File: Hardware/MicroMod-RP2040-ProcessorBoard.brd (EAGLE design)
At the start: 22 x 22 mm, 47 parts, among them J1 MICROMOD-2222, U1 W25QXX128MBIT, U2 FSUSB30MUX_MSOP10, U3 RP2040, Y1 12MHz

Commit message: Rename nets to match MicroMod nomenclature
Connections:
- net ADC0 renamed A0
- net ADC1 renamed A1
- net GPIO0 renamed G0
- net GPIO1 renamed G1
- net GPIO2 renamed G2
- net GPIO3 renamed G3
- net GPIO9 renamed G9
- net SPI_!CS!/GPIO5 renamed SPI_!CS!/G5
- net SPI_CIPO/GPIO4 renamed SPI_CIPO/G4
- net SPI_COPI/GPIO7 renamed SPI_COPI/G7
- net SPI_SCK/GPIO6 renamed SPI_SCK/G6
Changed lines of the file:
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@@
 <layers>
 <layer number="1" name="Top" color="4" fill="1" visible="yes" active="yes"/>
-<layer number="2" name="Horz" color="1" fill="3" visible="yes" active="yes"/>
-<layer number="15" name="Vert" color="4" fill="6" visible="yes" active="yes"/>
+<layer number="2" name="Horz" color="1" fill="3" visible="no" active="yes"/>
+<layer number="15" name="Vert" color="4" fill="6" visible="no" active="yes"/>
 <layer number="16" name="Bottom" color="1" fill="1" visible="yes" active="yes"/>
 <layer number="17" name="Pads" color="2" fill="1" visible="yes" active="yes"/>
@@
 <layer number="23" name="tOrigins" color="15" fill="1" visible="yes" active="yes"/>
 <layer number="24" name="bOrigins" color="15" fill="1" visible="yes" active="yes"/>
-<layer number="25" name="tNames" color="7" fill="1" visible="yes" active="yes"/>
-<layer number="26" name="bNames" color="7" fill="1" visible="yes" active="yes"/>
-<layer number="27" name="tValues" color="7" fill="1" visible="yes" active="yes"/>
-<layer number="28" name="bValues" color="7" fill="1" visible="yes" active="yes"/>
-<layer number="29" name="tStop" color="7" fill="3" visible="yes" active="yes"/>
-<layer number="30" name="bStop" color="7" fill="6" visible="yes" active="yes"/>
-<layer number="31" name="tCream" color="7" fill="4" visible="yes" active="yes"/>
-<layer number="32" name="bCream" color="7" fill="5" visible="yes" active="yes"/>
-<layer number="33" name="tFinish" color="6" fill="3" visible="yes" active="yes"/>
-<layer number="34" name="bFinish" color="6" fill="6" visible="yes" active="yes"/>
-<layer number="35" name="tGlue" color="7" fill="4" visible="yes" active="yes"/>
-<layer number="36" name="bGlue" color="7" fill="5" visible="yes" active="yes"/>
-<layer number="37" name="tTest" color="7" fill="1" visible="yes" active="yes"/>
-<layer number="38" name="bTest" color="7" fill="1" visible="yes" active="yes"/>
-<layer number="39" name="tKeepout" color="4" fill="11" visible="yes" active="yes"/>
-<layer number="40" name="bKeepout" color="1" fill="11" visible="yes" active="yes"/>
-<layer number="41" name="tRestrict" color="4" fill="10" visible="yes" active="yes"/>
-<layer number="42" name="bRestrict" color="1" fill="10" visible="yes" active="yes"/>
-<layer number="43" name="vRestrict" color="2" fill="10" visible="yes" active="yes"/>
-<layer number="44" name="Drills" color="7" fill="1" visible="yes" active="yes"/>
+<layer number="25" name="tNames" color="7" fill="1" visible="no" active="yes"/>
+<layer number="26" name="bNames" color="7" fill="1" visible="no" active="yes"/>
+<layer number="27" name="tValues" color="7" fill="1" visible="no" active="yes"/>
+<layer number="28" name="bValues" color="7" fill="1" visible="no" active="yes"/>
+<layer number="29" name="tStop" color="7" fill="3" visible="no" active="yes"/>
+<layer number="30" name="bStop" color="7" fill="6" visible="no" active="yes"/>
+<layer number="31" name="tCream" color="7" fill="4" visible="no" active="yes"/>
+<layer number="32" name="bCream" color="7" fill="5" visible="no" active="yes"/>
+<layer number="33" name="tFinish" color="6" fill="3" visible="no" active="yes"/>
+<layer number="34" name="bFinish" color="6" fill="6" visible="no" active="yes"/>
+<layer number="35" name="tGlue" color="7" fill="4" visible="no" active="yes"/>
+<layer number="36" name="bGlue" color="7" fill="5" visible="no" active="yes"/>
+<layer number="37" name="tTest" color="7" fill="1" visible="no" active="yes"/>
+<layer number="38" name="bTest" color="7" fill="1" visible="no" active="yes"/>
+<layer number="39" name="tKeepout" color="4" fill="11" visible="no" active="yes"/>
+<layer number="40" name="bKeepout" color="1" fill="11" visible="no" active="yes"/>
+<layer number="41" name="tRestrict" color="4" fill="10" visible="no" active="yes"/>
+<layer number="42" name="bRestrict" color="1" fill="10" visible="no" active="yes"/>
+<layer number="43" name="vRestrict" color="2" fill="10" visible="no" active="yes"/>
+<layer number="44" name="Drills" color="7" fill="1" visible="no" active="yes"/>
 <layer number="45" name="Holes" color="7" fill="1" visible="yes" active="yes"/>
-<layer number="46" name="Milling" color="3" fill="1" visible="yes" active="yes"/>
-<layer number="47" name="Measures" color="7" fill="1" visible="yes" active="yes"/>
-<layer number="48" name="Document" color="7" fill="1" visible="yes" active="yes"/>
-<layer number="49" name="Reference" color="7" fill="1" visible="yes" active="yes"/>
-<layer number="50" name="dxf" color="7" fill="1" visible="yes" active="yes"/>
+<layer number="46" name="Milling" color="3" fill="1" visible="no" active="yes"/>
+<layer number="47" name="Measures" color="7" fill="1" visible="no" active="yes"/>
+<layer number="48" name="Document" color="7" fill="1" visible="no" active="yes"/>
+<layer number="49" name="Reference" color="7" fill="1" visible="no" active="yes"/>
+<layer number="50" name="dxf" color="7" fill="1" visible="no" active="yes"/>
 <layer number="51" name="tDocu" color="6" fill="1" visible="yes" active="yes"/>
-<layer number="52" name="bDocu" color="7" fill="1" visible="yes" active="yes"/>
+<layer number="52" name="bDocu" color="7" fill="1" visible="no" active="yes"/>
 <layer number="91" name="Nets" color="2" fill="1" visible="no" active="no"/>
 <layer number="92" name="Busses" color="1" fill="1" visible="no" active="no"/>
@@
 <wire x1="14.9904" y1="5.541375" x2="15.25" y2="5.800975" width="0.127" layer="1"/>
 </signal>
-<signal name="SPI_SCK/GPIO6" class="1">
+<signal name="SPI_SCK/G6" class="1">
 <contactref element="J1" pad="57"/>
 <contactref element="U3" pad="34"/>
@@
 <wire x1="6.25" y1="5.46193125" x2="6.3" y2="5.51193125" width="0.127" layer="1"/>
 </signal>
-<signal name="SPI_COPI/GPIO7" class="1">
+<signal name="SPI_COPI/G7" class="1">
 <contactref element="J1" pad="59"/>
 <contactref element="U3" pad="35"/>
@@
 <wire x1="8.25" y1="1.275" x2="8.25" y2="3.7912" width="0.127" layer="1"/>
 </signal>
-<signal name="ADC0">
+<signal name="A0">
 <contactref element="J1" pad="34"/>
 <contactref element="U3" pad="38"/>
@@
 <wire x1="12.1587" y1="5.458625" x2="12.1587" y2="7.6413" width="0.127" layer="16"/>
 </signal>
-<signal name="ADC1">
+<signal name="A1">
 <contactref element="J1" pad="38"/>
 <contactref element="U3" pad="39"/>
@@
 <wire x1="3.5" y1="2.8633625" x2="2.9413" y2="3.4220625" width="0.127" layer="16"/>
 </signal>
-<signal name="SPI_CIPO/GPIO4" class="1">
+<signal name="SPI_CIPO/G4" class="1">
 <contactref element="J1" pad="61"/>
 <contactref element="U3" pad="31"/>
@@
 <wire x1="19" y1="13.1" x2="19" y2="12.25" width="0.127" layer="16"/>
 </signal>
-<signal name="SPI_!CS!/GPIO5" class="1">
+<signal name="SPI_!CS!/G5" class="1">
 <contactref element="J1" pad="55"/>
 <contactref element="U3" pad="32"/>
@@
 <wire x1="6.80530625" y1="3.90425625" x2="6.5825" y2="4.1270625" width="0.127" layer="16"/>
 </signal>
-<signal name="GPIO1" class="1">
+<signal name="G1" class="1">
 <contactref element="J1" pad="42"/>
 <contactref element="U3" pad="28"/>
@@
 <wire x1="10.1952" y1="3.23585625" x2="10.1952" y2="2.7952" width="0.127" layer="16"/>
 </signal>
-<signal name="GPIO3" class="1">
+<signal name="G3" class="1">
 <contactref element="J1" pad="46"/>
 <contactref element="U3" pad="30"/>
@@
 <wire x1="7.9" y1="7.6" x2="7.75" y2="7.75" width="0.127" layer="16"/>
 </signal>
-<signal name="GPIO2" class="1">
+<signal name="G2" class="1">
 <contactref element="J1" pad="44"/>
 <contactref element="U3" pad="29"/>
@@
 <wire x1="8.7952" y1="8.97374375" x2="8.59954375" y2="9.1694" width="0.127" layer="16"/>
 </signal>
-<signal name="GPIO0" class="1">
+<signal name="G0" class="1">
 <contactref element="J1" pad="40"/>
 <contactref element="U3" pad="27"/>
@@
 <wire x1="19.5" y1="14" x2="18.5" y2="14" width="0.127" layer="16"/>
 </signal>
-<signal name="GPIO9">
+<signal name="G9">
 <contactref element="J1" pad="65"/>
 <contactref element="U3" pad="40"/>

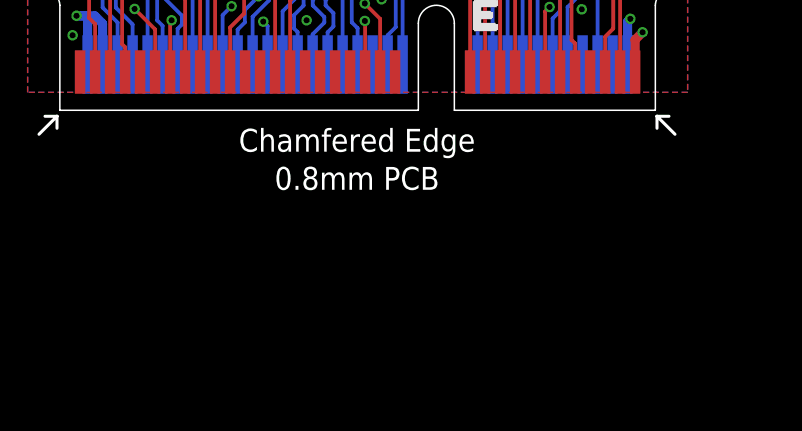
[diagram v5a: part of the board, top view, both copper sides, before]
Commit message: Update Schematic (PDF) and Add Dimensions in BRD File
- regenerate schematic with updated nets based on MicroMod nomenclature
- Add board measurements in dimensions layer
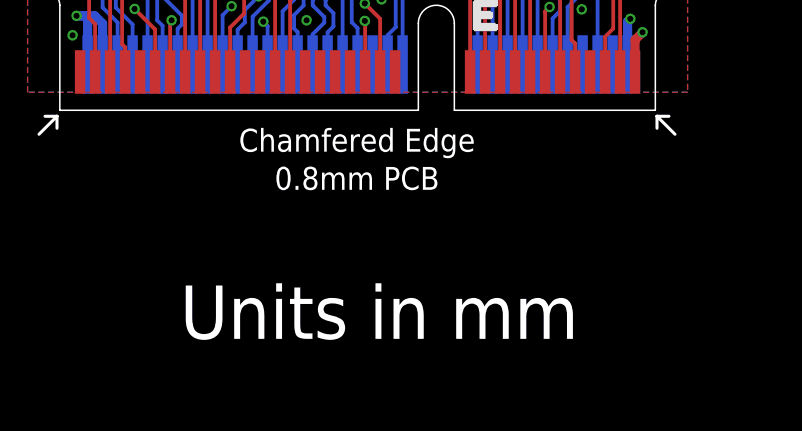
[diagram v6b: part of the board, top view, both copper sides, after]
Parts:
- moved LOGO4 6.35 mm to (30.9, 50.8)
- moved FRAME1 6.35 mm to (-8.89, -15.2)
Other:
- board text added: "Units in mm"
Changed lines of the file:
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@@
 <?xml version="1.0" encoding="utf-8"?>
 <!DOCTYPE eagle SYSTEM "eagle.dtd">
-<eagle version="9.6.2">
+<eagle version="9.4.2">
 <drawing>
 <settings>
-<setting alwaysvectorfont="yes"/>
+<setting alwaysvectorfont="no"/>
 <setting verticaltext="up"/>
 </settings>
@@
 <wire x1="0" y1="4.6" x2="0.6" y2="4" width="0.05" layer="20" curve="86.784874"/>
 <wire x1="21.4" y1="4" x2="22" y2="4.6" width="0.05" layer="20" curve="86.784874"/>
-<text x="27.81" y="31.67" size="1.778" layer="51" font="vector" ratio="15">0.8mm PCB
+<text x="34.16" y="31.67" size="1.778" layer="51" font="vector" ratio="15">0.8mm PCB
 45 degree chamfered edge
 Four layer design</text>
@@
 <wire x1="0" y1="4.6" x2="0.6" y2="4" width="0.05" layer="20" curve="86.784874"/>
 <text x="19.5" y="21" size="0.762" layer="16" font="vector" ratio="15" rot="SMR0" align="center">v10</text>
-<text x="17.78" y="-8.89" size="1.778" layer="51" font="vector" ratio="15">N. Seidle</text>
+<text x="17.78" y="-15.24" size="1.778" layer="51" font="vector" ratio="15">N. Seidle</text>
 <wire x1="13.25" y1="22" x2="16.75" y2="22" width="0.05" layer="20" curve="180"/>
+<dimension x1="1.075" y1="0" x2="13.025" y2="0" x3="7.05" y3="-2.54" textsize="1.778" layer="20"/>
+<dimension x1="14.225" y1="0" x2="20.925" y2="0" x3="17.575" y3="-3.81" textsize="1.778" layer="20"/>
+<dimension x1="0" y1="22" x2="22" y2="22" x3="11" y3="24.13" textsize="1.778" layer="20" dtype="horizontal"/>
+<dimension x1="20.925" y1="0" x2="22" y2="22" x3="25.4" y3="11" textsize="1.778" layer="20" dtype="vertical"/>
+<text x="5.08" y="-7.62" size="1.778" layer="20" font="vector" ratio="15">Units in mm</text>
 </plain>
 <attributes>
@@
 </autorouter>
 <elements>
-<element name="FRAME1" library="SparkFun-Aesthetics" package="CREATIVE_COMMONS" value="FRAME-LEDGER" x="-8.89" y="-8.89" smashed="yes">
-<attribute name="DESIGNER" value="" x="-8.89" y="-8.89" size="1.778" layer="27" font="vector" ratio="15" display="off"/>
-<attribute name="REV" value="" x="-8.89" y="-8.89" size="1.778" layer="27" font="vector" ratio="15" display="off"/>
+<element name="FRAME1" library="SparkFun-Aesthetics" package="CREATIVE_COMMONS" value="FRAME-LEDGER" x="-8.89" y="-15.24" smashed="yes">
+<attribute name="DESIGNER" value="" x="-8.89" y="-15.24" size="1.778" layer="27" font="vector" ratio="15" display="off"/>
+<attribute name="REV" value="" x="-8.89" y="-15.24" size="1.778" layer="27" font="vector" ratio="15" display="off"/>
 </element>
 <element name="C11" library="SparkFun-Capacitors" package="0402-TIGHT" value="15pF" x="3" y="10" smashed="yes">
@@
 <element name="FD4" library="SparkFun-Aesthetics" package="FIDUCIAL-MICRO" value="FIDUCIALUFIDUCIAL" x="1" y="5" smashed="yes" rot="MR0"/>
 <element name="LOGO3" library="SparkFun-Aesthetics" package="OSHW-LOGO-MINI" value="OSHW-LOGOMINI" x="19.746" y="18.701" smashed="yes" rot="MR90"/>
-<element name="LOGO4" library="SparkFun-Aesthetics" package="ORDERING_INSTRUCTIONS" value="SPECIAL_INSTRUCTIONS-ORDERING" x="24.54" y="50.8" smashed="yes"/>
+<element name="LOGO4" library="SparkFun-Aesthetics" package="ORDERING_INSTRUCTIONS" value="SPECIAL_INSTRUCTIONS-ORDERING" x="30.89" y="50.8" smashed="yes"/>
 <element name="J1" library="SparkFun-MicroMod" package="M.2-CARD-E-22" value="MICROMOD-2222" x="11" y="0" smashed="yes"/>
 <element name="LOGO1" library="SparkFun-Aesthetics" package="SFE_LOGO_NAME_FLAME_.1" value="SFE_LOGO_NAME_FLAME.1_INCH" x="1.7" y="11.2" smashed="yes" rot="MR90"/>
